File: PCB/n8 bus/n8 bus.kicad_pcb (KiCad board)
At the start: 2 copper layers, 76.2 x 43.2 mm, 1 part, among them J1 n8 Bus Connector

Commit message: n8 bus card template updated
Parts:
- J1: moved to F.Cu
- moved J1 37.1 mm to (147.2, 112.5)
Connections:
- J1 pad 1: +5V -> GND
- J1 pad 10: /D2 -> ~RES
- J1 pad 11: /A3 -> ~IRQ
- J1 pad 12: /D3 -> CLK
- J1 pad 13: /A4 -> /D7
- J1 pad 14: /D4 -> R~W
- J1 pad 15: /A5 -> /D6
- J1 pad 16: /D5 -> ~CS
- J1 pad 17: ~CS -> /D5
- J1 pad 18: /D6 -> /A5
- J1 pad 19: R~W -> /D4
- J1 pad 2: +5V -> GND
- J1 pad 20: /D7 -> /A4
- J1 pad 21: CLK -> /D3
- J1 pad 22: ~IRQ -> /A3
- J1 pad 23: ~RES -> /D2
- J1 pad 24: ~NMI -> /A2
- J1 pad 25: FUTURE0 -> /D1
- J1 pad 26: USB_D+ -> /A1
- J1 pad 27: FUTURE1 -> /D0
- J1 pad 28: USB_D- -> /A0
- J1 pad 29: +5V -> GND
- J1 pad 3: GND -> +5V
- J1 pad 30: +5V -> GND
- J1 pad 31: GND -> +5V
- J1 pad 32: GND -> +5V
- J1 pad 4: GND -> +5V
- J1 pad 5: /A0 -> ~WRITE
- J1 pad 6: /D0 -> FUTURE1
- J1 pad 7: /A1 -> ~READ
- J1 pad 8: /D1 -> FUTURE0
- J1 pad 9: /A2 -> ~NMI

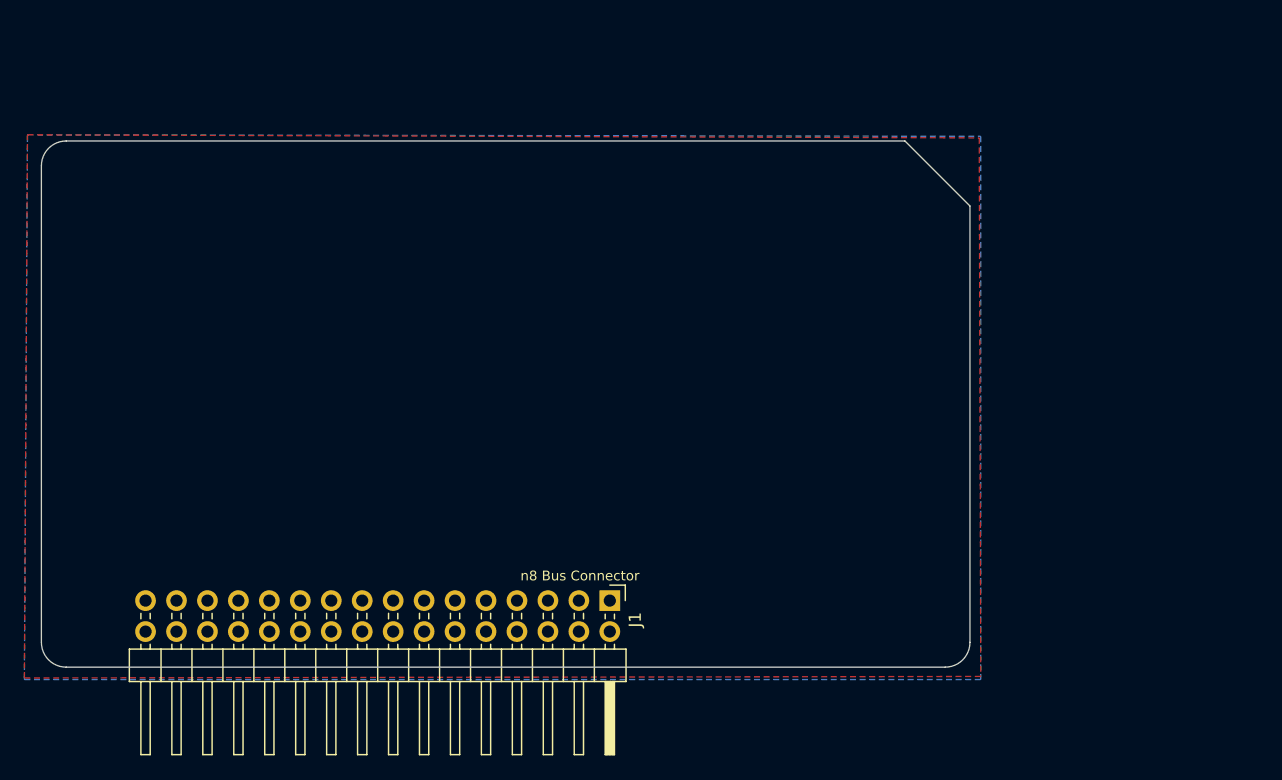
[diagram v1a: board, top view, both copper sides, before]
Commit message: Start of VDP based gfx card
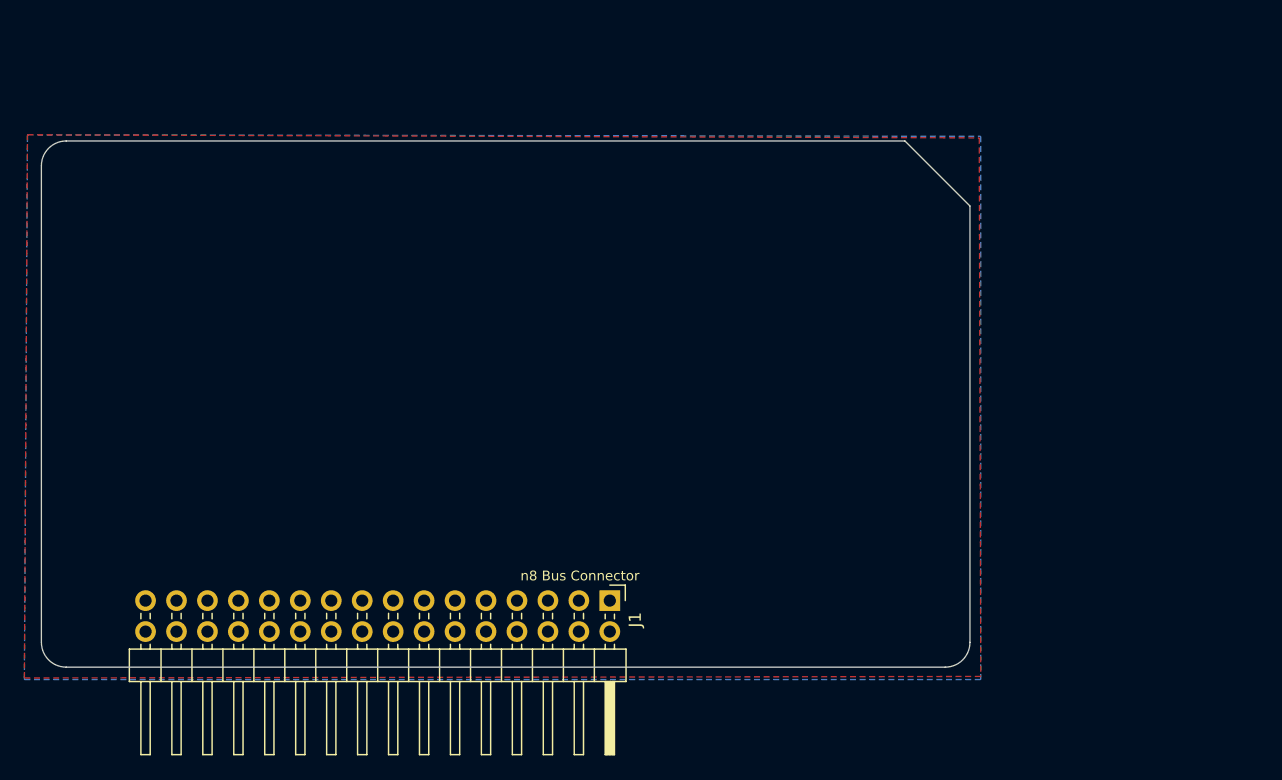
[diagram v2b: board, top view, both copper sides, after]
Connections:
- net R~W renamed R~{W}
- net ~CS renamed ~{CS}
- net ~IRQ renamed ~{IRQ}
- net ~NMI renamed ~{NMI}
- net ~READ renamed ~{READ}
- net ~RES renamed ~{RES}
- net ~WRITE renamed ~{WRITE}
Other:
- net class Default removed

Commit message: added 2 new soundcard designs
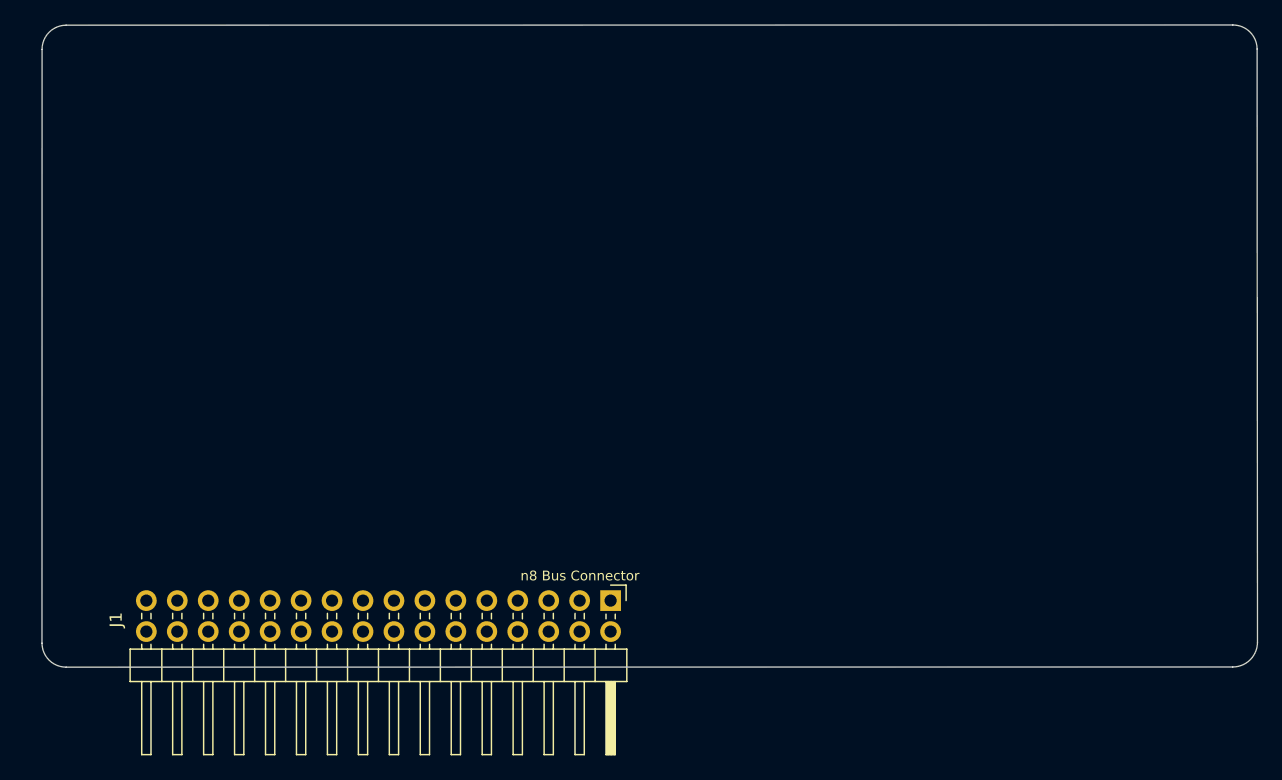
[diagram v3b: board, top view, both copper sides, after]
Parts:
- moved J1 0.07 mm to (147.3, 112.5)
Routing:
- removed copper zone on B.Cu, net (none)
- removed copper zone on F.Cu, net (none)
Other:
- board size 76.2 x 43.2 mm -> 99.7 x 52.7 mm
